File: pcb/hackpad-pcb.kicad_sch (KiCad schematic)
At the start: 50 parts, among them J1 OLED_128x32, U1 MCU_Seeed_XIAO_RP2040

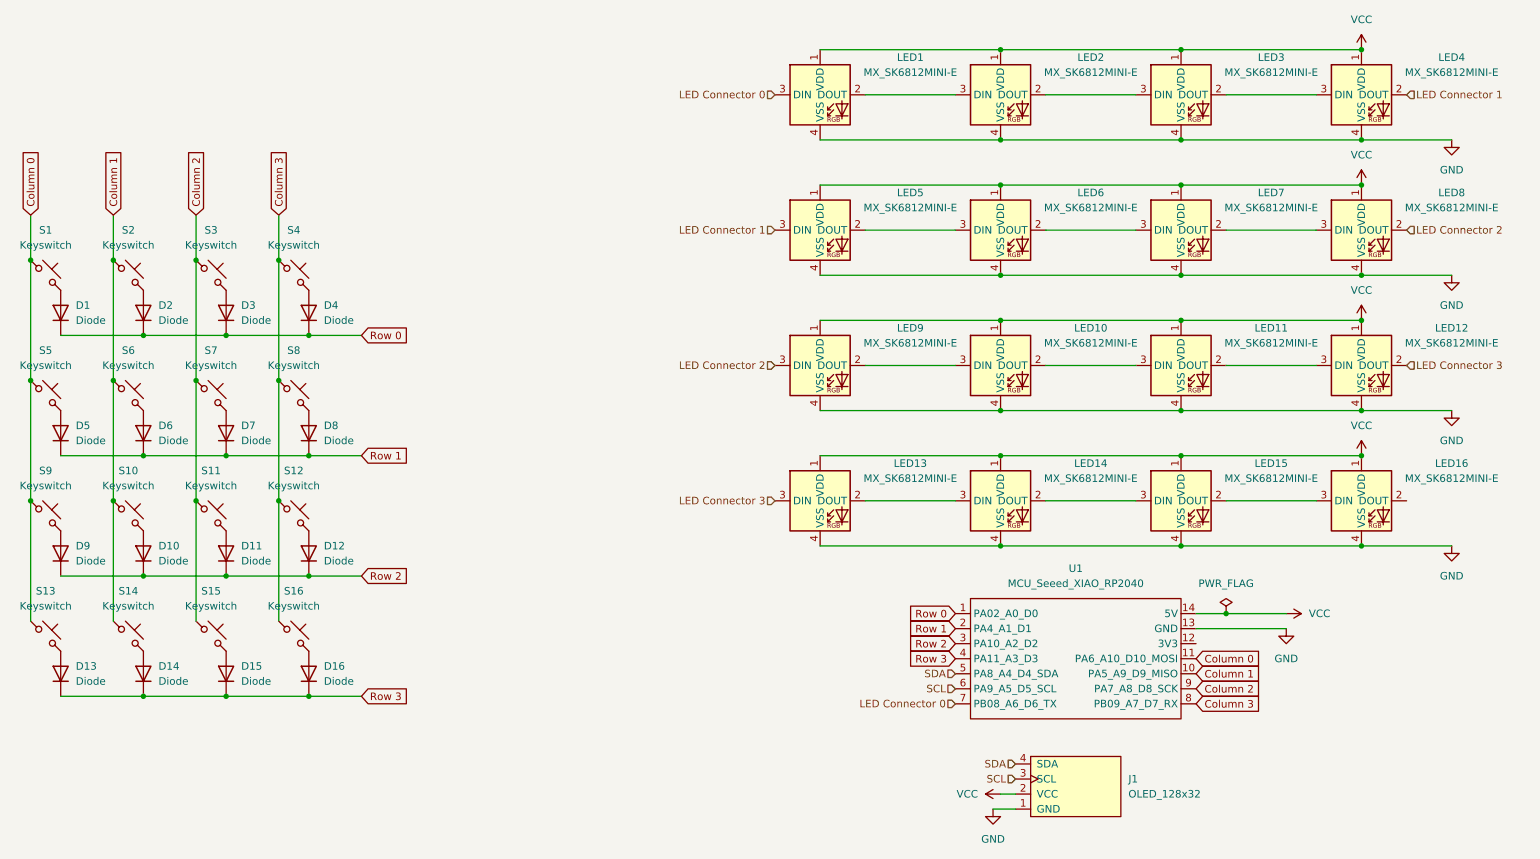
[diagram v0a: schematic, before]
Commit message: Replaced neopixels with simple 2x3x4 mm leds to avoid smd soldering
Signed-off-by: Urjith Mishra <66270347+TheScientist101@users.noreply.github.com>
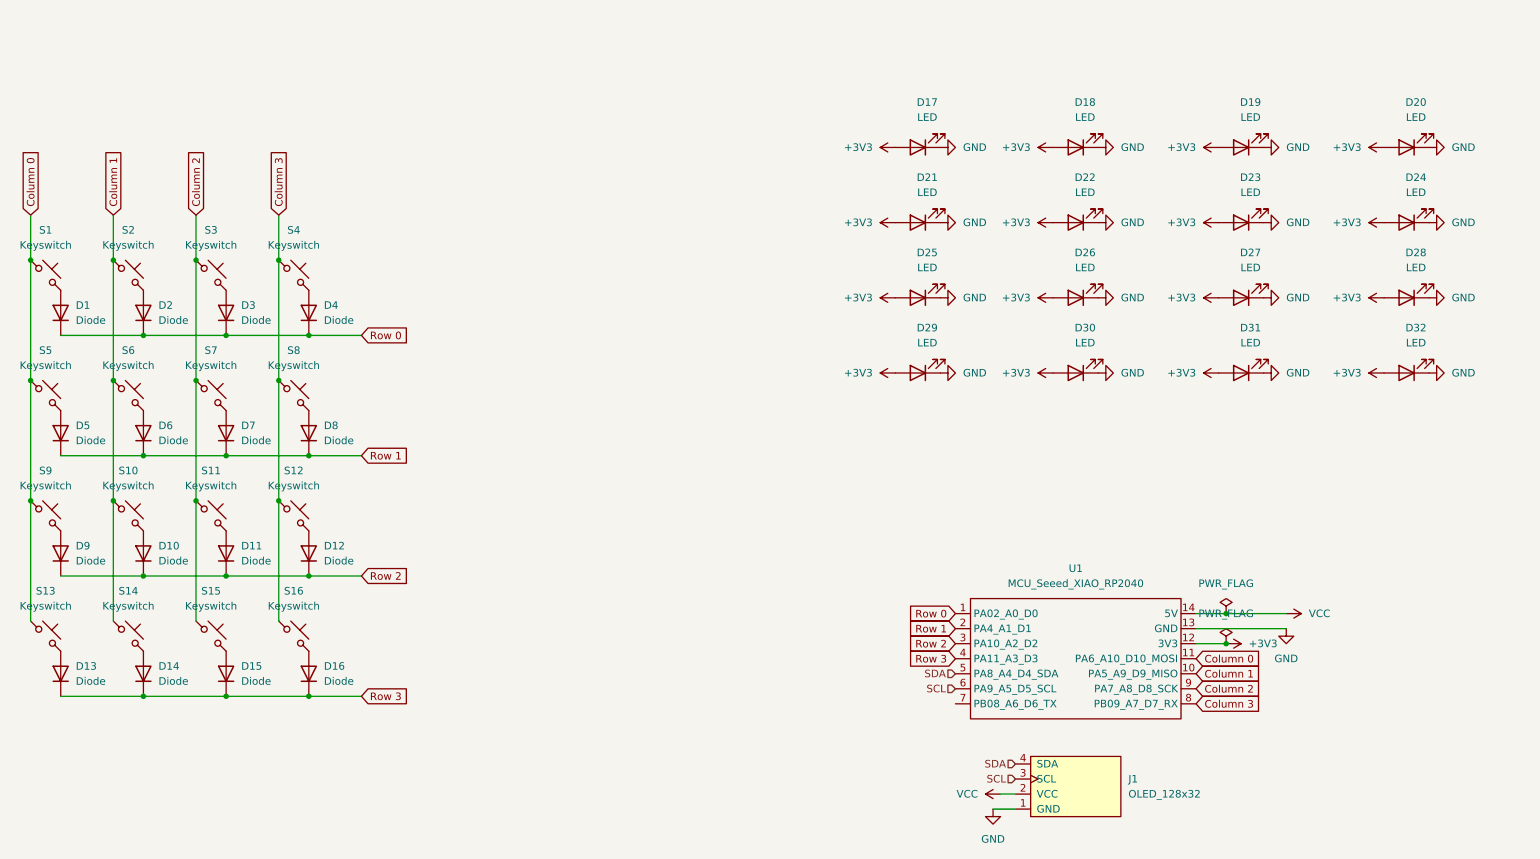
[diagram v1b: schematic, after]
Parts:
- removed LED1, LED10, LED11, LED12, LED13, LED14, LED15, LED16, LED2, LED3, LED4, LED5, LED6, LED7, LED8, LED9: MX_SK6812MINI-E, PCM_marbastlib-mx:LED_MX_6028R, symbol PCM_marbastlib-mx:MX_SK6812MINI-E
- added D17, D18, D19, D20, D21, D22, D23, D24, D25, D26, D27, D28, D29, D30, D31, D32: LED, PCM_marbastlib-mx:LED_MX_3mm-ROT, symbol Device:LED
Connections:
- net GND: now also D17.1 (K), D18.1 (K), D19.1 (K), D20.1 (K), D21.1 (K), D22.1 (K), D23.1 (K), D24.1 (K), D25.1 (K), D26.1 (K), D27.1 (K), D28.1 (K), D29.1 (K), D30.1 (K), D31.1 (K), D32.1 (K)
- net +3V3: now reaches U1.12 (3V3)
- net +3V3: now also D17.2 (A), D18.2 (A), D19.2 (A), D20.2 (A), D21.2 (A), D22.2 (A), D23.2 (A), D24.2 (A), D25.2 (A), D26.2 (A), D27.2 (A), D28.2 (A), D29.2 (A), D30.2 (A), D31.2 (A), D32.2 (A)
- net LED Connector 0: no longer names the net of U1.7 (PB08_A6_D6_TX)
